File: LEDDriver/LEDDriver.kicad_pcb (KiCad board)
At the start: 2 copper layers, 39.4 x 41.9 mm, 16 parts, among them CON1 36V DC Power, P1 En, P2 ToLED, P3 To5V Power, Q1 Q_PMOS_GDS

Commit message: lestarch: adding design files for combined design v2.0
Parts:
- removed C2: Cf, Capacitors_SMD:C_0805
- removed C3: Cin, Capacitors_SMD:C_0603
- removed C4: CP, Capacitors_ThroughHole:C_Radial_D10_L16_P5
- removed CON1: 36V DC Power, footprints:PJ-051A
- removed D1: D_Schottky, Diodes_ThroughHole:Diode_DO-41_SOD81_Horizontal_RM10
- removed L1: INDUCTOR, footprints:SLF6045
- removed LM1: lm3409, Housings_DIP:DIP-14_W7.62mm
- removed P1: En, Pin_Headers:Pin_Header_Straight_1x01
- removed P2: ToLED, Pin_Headers:Pin_Header_Straight_1x02
- removed P3: To5V Power, Pin_Headers:Pin_Header_Straight_1x02
- removed Q1: Q_PMOS_GDS, footprints:TO-252-3
- removed R1: Roff, Resistors_SMD:R_1210
- removed R2: Ruv1, Resistors_SMD:R_1210
- removed R3: Ruv2, Resistors_SMD:R_0805
- removed R4: Rsns, footprints:R_1020
- added 110u: CP, Capacitors_ThroughHole:C_Radial_D10_L16_P5, F.Cu at (162.6, 88.9)
- added 1k: R, Resistors_SMD:R_0402, F.Cu at (142.2, 104.8)
- added 1k: R, Resistors_SMD:R_0402, F.Cu at (144.1, 104.8)
- added 30V,GND: ToLED, Pin_Headers:Pin_Header_Straight_1x02, F.Cu at (165.7, 112.4)
- added 330u: 330u, Capacitors_ThroughHole:C_Radial_D10_L16_P5, F.Cu at (135.9, 76.2)
- added 36V DC: 36V DC Power, footprints:PJ-051A, F.Cu at (163.2, 76.2)
- added 5V,GND: FanOut, Pin_Headers:Pin_Header_Straight_1x02, F.Cu at (129.5, 111.8)
- added Cf: Cf, Capacitors_SMD:C_0805, F.Cu at (156.8, 90.8)
- added Cin: Cin, Capacitors_SMD:C_0603, F.Cu at (156.8, 87.0)
- added D: D_Schottky, Diodes_ThroughHole:Diode_DO-41_SOD81_Horizontal_RM10, F.Cu at (168.3, 107.3)
- added D: D_Schottky, Diodes_ThroughHole:Diode_DO-41_SOD81_Horizontal_RM10, F.Cu at (144.1, 84.5)
- added Fan,LED,GND,5V: TeensyConnector, Pin_Headers:Pin_Header_Straight_1x04, F.Cu at (129.5, 92.1)
- added L15u: INDUCTOR, footprints:SLF6045, F.Cu at (159.4, 109.9)
- added L330u: 330u, Resistors_ThroughHole:Resistor_Horizontal_RM25mm, F.Cu at (136.5, 84.5)
- added NMOS: Q_NMOS_GDS, footprints:TO-252-3, F.Cu at (144.1, 110.5)
- added PMOS: Q_PMOS_GDS, footprints:TO-252-3, F.Cu at (163.2, 102.2)
- added Roff: Roff, Resistors_SMD:R_1210, F.Cu at (153.7, 111.1)
- added Rsns: Rsns, footprints:R_1020, F.Cu at (159.4, 96.5)
- added Ruv1: Ruv1, Resistors_SMD:R_1210, F.Cu at (151.1, 83.8)
- added Ruv2: Ruv2, Resistors_SMD:R_0805, F.Cu at (155.6, 83.8)
- added TL2575: TL25527, footprints:TO-263, F.Cu at (154.3, 76.2)
- added lm3409: lm3409, Housings_DIP:DIP-14_W7.62mm, F.Cu at (146.7, 89.5)
- moved C1 33.6 mm to (144.8, 101.6)
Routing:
- net /Regulator1/5VOut: track 0.00 -> 88.5 mm
- net VCC: track 75.7 -> 36.8 mm
- net Net-(D201-Pad1): track 0.00 -> 21.6 mm
- net Net-(P3-Pad4): track 0.00 -> 17.0 mm
- net Net-(Q2-Pad1): track 0.00 -> 13.3 mm
- net Net-(P1-Pad2): track 0.00 -> 12.6 mm
- net Net-(LM1-Pad4): track 5.08 -> 17.1 mm
- net GND: track 155.8 -> 147.2 mm, vias 3 -> 6
- net Net-(D1-Pad1): track 9.04 -> 16.7 mm
- net Net-(C1-Pad1): track 10.3 -> 17.2 mm
- net Net-(LM1-Pad1): track 14.1 -> 12.1 mm
- net Net-(C2-Pad2): track 4.45 -> 3.86 mm
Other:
- board size 39.4 x 41.9 mm -> 44.5 x 46.4 mm
- net class Default: trace_width 0.25 -> 0.5; via_dia 0.6 -> 0.8
- rule pad_to_mask_clearance: 0.2 -> 0
- board text added: "LeStarch 2016 - Combined circuit for micro- controller driven LED lamp. - LED Driver 30V, 1A - Regulator 5V, ~1A - NMOS GND switch"
- board text removed: "LED driver: Vin - 36V, Vout - 30V, Iout - 1A LEDs need a constant current and thus cannot be driven given just a voltage, but rather must be driven to maintain constant current."
- board text removed: "LeStarch 2015"

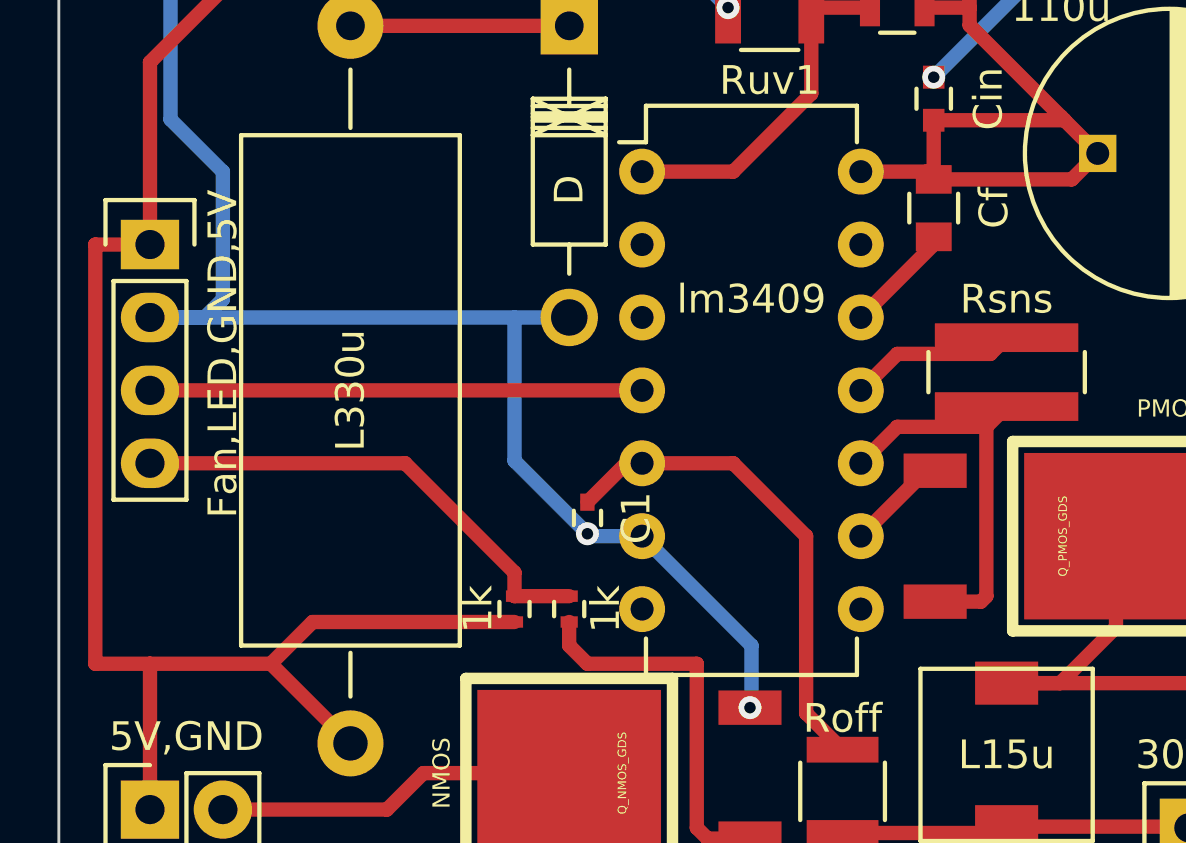
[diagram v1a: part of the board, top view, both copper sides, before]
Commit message: lestarch: changing resistors to pulldown resistors; adding pulldown to LED
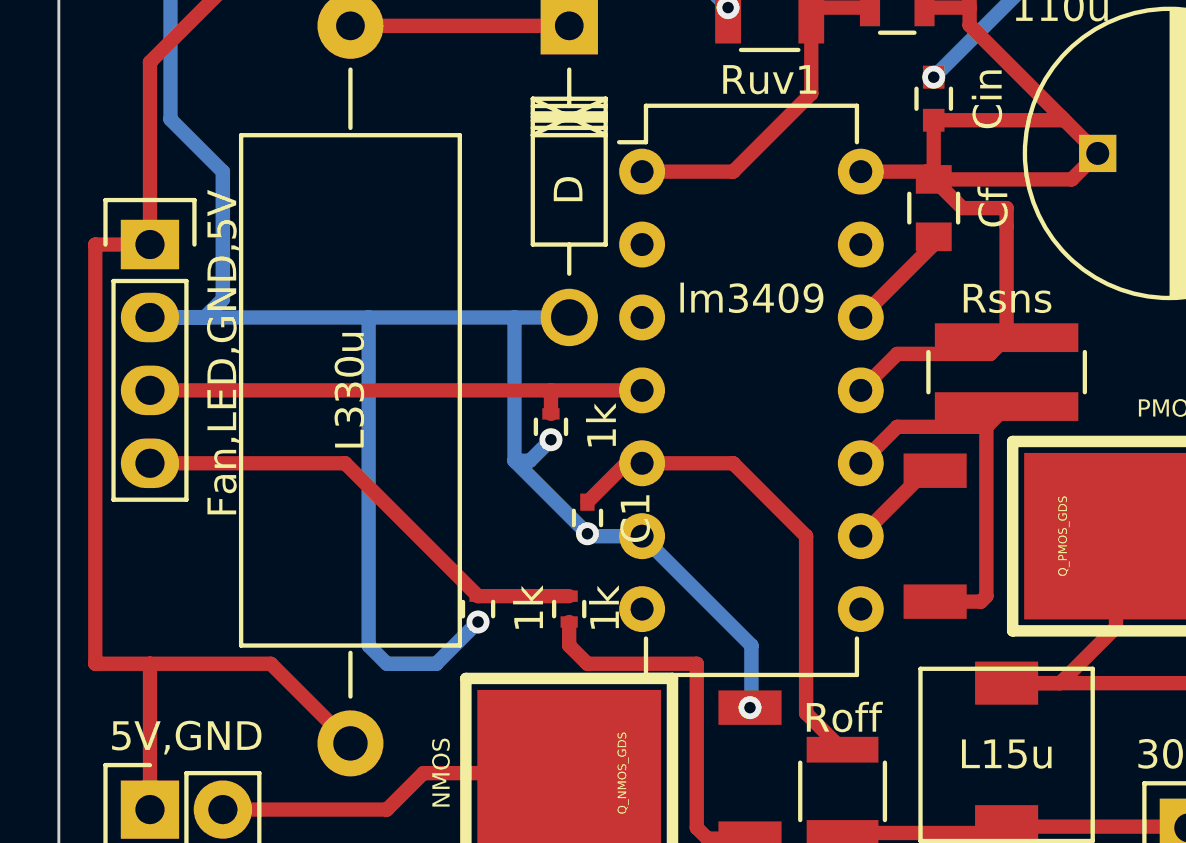
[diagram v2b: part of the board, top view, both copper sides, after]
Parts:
- removed the 1k at (142.2, 104.8)
- added 1k: R, Resistors_SMD:R_0402, F.Cu at (141.0, 104.8)
- added 1k: R, Resistors_SMD:R_0402, F.Cu at (143.5, 98.4)
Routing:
- net GND: track 147.2 -> 164.9 mm, vias 6 -> 8
- net /Regulator1/5VOut: track 88.5 -> 79.4 mm
- net VCC: track 36.8 -> 44.2 mm
- net Net-(LM1-Pad4): track 17.1 -> 18.0 mm
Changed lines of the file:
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@@
 (kicad_pcb (version 4) (host pcbnew 4.0.4+e1-6308~48~ubuntu16.04.1-stable)
   (general
-    (links 46)
-    (no_connects 1)
-    (area 114.846904 20.03 163.63246 65.890476)
+    (links 48)
+    (no_connects 0)
+    (area 126.314999 68.529999 170.865001 114.985001)
     (thickness 1.6)
     (drawings 6)
-    (tracks 131)
+    (tracks 143)
     (zones 0)
-    (modules 23)
+    (modules 24)
     (nets 21)
   )
@@
   (layers
     (0 F.Cu signal)
-    (31 B.Cu signal hide)
+    (31 B.Cu signal)
     (32 B.Adhes user hide)
     (33 F.Adhes user hide)
     (34 B.Paste user hide)
     (35 F.Paste user hide)
-    (36 B.SilkS user)
+    (36 B.SilkS user hide)
     (37 F.SilkS user)
     (38 B.Mask user hide)
@@
     (add_net "Net-(Q2-Pad1)")
     (add_net VCC)
+  )
+  (module Resistors_SMD:R_0402 (layer F.Cu)
+    (at 140.97 104.775 270)
+    (descr "Resistor SMD 0402, reflow soldering, Vishay (see dcrcw.pdf)")
+    (tags "resistor 0402")
+    (attr smd)
+    (fp_text reference 1k (at 0 -1.8 270) (layer F.SilkS)
+      (effects (font (size 1 1) (thickness 0.15)))
+    )
+    (fp_text value R (at 0 1.8 270) (layer F.Fab)
+      (effects (font (size 1 1) (thickness 0.15)))
+    )
+    (fp_line (start -0.95 -0.65) (end 0.95 -0.65) (layer F.CrtYd) (width 0.05))
+    (fp_line (start -0.95 0.65) (end 0.95 0.65) (layer F.CrtYd) (width 0.05))
+    (fp_line (start -0.95 -0.65) (end -0.95 0.65) (layer F.CrtYd) (width 0.05))
+    (fp_line (start 0.95 -0.65) (end 0.95 0.65) (layer F.CrtYd) (width 0.05))
+    (fp_line (start 0.25 -0.525) (end -0.25 -0.525) (layer F.SilkS) (width 0.15))
+    (fp_line (start -0.25 0.525) (end 0.25 0.525) (layer F.SilkS) (width 0.15))
+    (pad 1 smd rect (at -0.45 0 270) (size 0.4 0.6) (layers F.Cu F.Paste F.Mask)
+      (net 19 "Net-(P3-Pad4)"))
+    (pad 2 smd rect (at 0.45 0 270) (size 0.4 0.6) (layers F.Cu F.Paste F.Mask)
+      (net 2 GND))
+    (model Resistors_SMD.3dshapes/R_0402.wrl
+      (at (xyz 0 0 0))
+      (scale (xyz 1 1 1))
+      (rotate (xyz 0 0 0))
+    )
   )
   (module Capacitors_SMD:C_0402 (layer F.Cu)
@@
   )
   (module Resistors_SMD:R_0402 (layer F.Cu)
-    (at 142.24 104.775 270)
-    (descr "Resistor SMD 0402, reflow soldering, Vishay (see dcrcw.pdf)")
-    (tags "resistor 0402")
-    (attr smd)
-    (fp_text reference 1k (at 0 1.27 270) (layer F.SilkS)
-      (effects (font (size 1 1) (thickness 0.15)))
-    )
-    (fp_text value R (at 0 1.8 270) (layer F.Fab)
-      (effects (font (size 1 1) (thickness 0.15)))
-    )
-    (fp_line (start -0.95 -0.65) (end 0.95 -0.65) (layer F.CrtYd) (width 0.05))
-    (fp_line (start -0.95 0.65) (end 0.95 0.65) (layer F.CrtYd) (width 0.05))
-    (fp_line (start -0.95 -0.65) (end -0.95 0.65) (layer F.CrtYd) (width 0.05))
-    (fp_line (start 0.95 -0.65) (end 0.95 0.65) (layer F.CrtYd) (width 0.05))
-    (fp_line (start 0.25 -0.525) (end -0.25 -0.525) (layer F.SilkS) (width 0.15))
-    (fp_line (start -0.25 0.525) (end 0.25 0.525) (layer F.SilkS) (width 0.15))
-    (pad 1 smd rect (at -0.45 0 270) (size 0.4 0.6) (layers F.Cu F.Paste F.Mask)
-      (net 19 "Net-(P3-Pad4)"))
-    (pad 2 smd rect (at 0.45 0 270) (size 0.4 0.6) (layers F.Cu F.Paste F.Mask)
-      (net 5 /Regulator1/5VOut))
-    (model Resistors_SMD.3dshapes/R_0402.wrl
-      (at (xyz 0 0 0))
-      (scale (xyz 1 1 1))
-      (rotate (xyz 0 0 0))
-    )
-  )
-  (module Resistors_SMD:R_0402 (layer F.Cu)
     (at 144.145 104.775 270)
     (descr "Resistor SMD 0402, reflow soldering, Vishay (see dcrcw.pdf)")
@@
     (pad "" smd rect (at 0 -10.67 90) (size 10.8 7) (layers F.Cu F.Paste F.Mask))
   )
+  (module Resistors_SMD:R_0402 (layer F.Cu)
+    (at 143.51 98.425 270)
+    (descr "Resistor SMD 0402, reflow soldering, Vishay (see dcrcw.pdf)")
+    (tags "resistor 0402")
+    (attr smd)
+    (fp_text reference 1k (at 0 -1.8 270) (layer F.SilkS)
+      (effects (font (size 1 1) (thickness 0.15)))
+    )
+    (fp_text value R (at 0 1.8 270) (layer F.Fab)
+      (effects (font (size 1 1) (thickness 0.15)))
+    )
+    (fp_line (start -0.95 -0.65) (end 0.95 -0.65) (layer F.CrtYd) (width 0.05))
+    (fp_line (start -0.95 0.65) (end 0.95 0.65) (layer F.CrtYd) (width 0.05))
+    (fp_line (start -0.95 -0.65) (end -0.95 0.65) (layer F.CrtYd) (width 0.05))
+    (fp_line (start 0.95 -0.65) (end 0.95 0.65) (layer F.CrtYd) (width 0.05))
+    (fp_line (start 0.25 -0.525) (end -0.25 -0.525) (layer F.SilkS) (width 0.15))
+    (fp_line (start -0.25 0.525) (end 0.25 0.525) (layer F.SilkS) (width 0.15))
+    (pad 1 smd rect (at -0.45 0 270) (size 0.4 0.6) (layers F.Cu F.Paste F.Mask)
+      (net 12 "Net-(LM1-Pad4)"))
+    (pad 2 smd rect (at 0.45 0 270) (size 0.4 0.6) (layers F.Cu F.Paste F.Mask)
+      (net 2 GND))
+    (model Resistors_SMD.3dshapes/R_0402.wrl
+      (at (xyz 0 0 0))
+      (scale (xyz 1 1 1))
+      (rotate (xyz 0 0 0))
+    )
+  )
   (gr_text "LeStarch 2016 -\n  Combined circuit for micro-\n  controller driven LED lamp.\n    - LED Driver 30V, 1A\n    - Regulator 5V, ~1A\n    - NMOS GND switch" (at 166.37 90.805) (layer B.SilkS)
     (effects (font (size 1.5 1.5) (thickness 0.3)) (justify left mirror))
@@
   (segment (start 146.685 99.695) (end 146.135 99.695) (width 0.5) (layer F.Cu) (net 1))
   (segment (start 146.135 99.695) (end 144.78 101.05) (width 0.5) (layer F.Cu) (net 1))
+  (via (at 140.97 105.225) (size 0.8) (drill 0.4) (layers F.Cu B.Cu) (net 2) (status C00000))
+  (segment (start 137.16 94.615) (end 137.16 106.045) (width 0.5) (layer B.Cu) (net 2))
+  (segment (start 137.795 106.68) (end 137.16 106.045) (width 0.5) (layer B.Cu) (net 2))
+  (segment (start 139.515 106.68) (end 137.795 106.68) (width 0.5) (layer B.Cu) (net 2))
+  (segment (start 139.515 106.68) (end 140.97 105.225) (width 0.5) (layer B.Cu) (net 2) (status 800000))
+  (via (at 143.51 98.875) (size 0.8) (drill 0.4) (layers F.Cu B.Cu) (net 2))
+  (segment (start 142.24 99.61) (end 142.775 99.61) (width 0.5) (layer B.Cu) (net 2))
+  (segment (start 142.775 99.61) (end 143.51 98.875) (width 0.5) (layer B.Cu) (net 2))
   (segment (start 146.05 82.55) (end 148.41 82.55) (width 0.5) (layer B.Cu) (net 2))
   (segment (start 148.41 82.55) (end 149.68 83.82) (width 0.5) (layer B.Cu) (net 2))
@@
   (segment (start 150.495 108.15828) (end 150.495 106.045) (width 0.5) (layer B.Cu) (net 2))
   (segment (start 146.685 102.235) (end 150.495 106.045) (width 0.5) (layer B.Cu) (net 2))
-  (segment (start 129.54 94.615) (end 142.24 94.615) (width 0.5) (layer B.Cu) (net 2))
+  (segment (start 129.54 94.615) (end 137.16 94.615) (width 0.5) (layer B.Cu) (net 2))
+  (segment (start 137.16 94.615) (end 142.24 94.615) (width 0.5) (layer B.Cu) (net 2))
   (segment (start 142.24 94.615) (end 144.14754 94.615) (width 0.5) (layer B.Cu) (net 2))
   (segment (start 130.255 82.55) (end 130.255 87.71) (width 0.5) (layer B.Cu) (net 2))
@@
   (via (at 154.305 76.2) (size 0.8) (drill 0.4) (layers F.Cu B.Cu) (net 2))
   (via (at 156.845 86.245) (size 0.8) (drill 0.4) (layers F.Cu B.Cu) (net 2))
+  (segment (start 159.385 90.805) (end 157.845 90.805) (width 0.5) (layer F.Cu) (net 3))
+  (segment (start 159.385 95.32) (end 159.385 91.44) (width 0.5) (layer F.Cu) (net 3))
+  (segment (start 159.385 90.805) (end 159.385 91.44) (width 0.5) (layer F.Cu) (net 3))
+  (segment (start 157.845 90.805) (end 156.845 89.805) (width 0.5) (layer F.Cu) (net 3))
   (segment (start 158.095 83.82) (end 156.525 83.82) (width 0.5) (layer F.Cu) (net 3))
   (segment (start 154.305 97.155) (end 155.575 95.885) (width 0.5) (layer F.Cu) (net 3))
@@
   (segment (start 156.845 91.805) (end 156.845 92.075) (width 0.5) (layer F.Cu) (net 4))
   (segment (start 156.845 92.075) (end 154.305 94.615) (width 0.5) (layer F.Cu) (net 4))
-  (segment (start 142.24 105.225) (end 135.20632 105.225) (width 0.5) (layer F.Cu) (net 5))
-  (segment (start 135.20632 105.225) (end 133.75132 106.68) (width 0.5) (layer F.Cu) (net 5))
   (segment (start 129.54 111.76) (end 129.54 106.68) (width 0.5) (layer F.Cu) (net 5))
   (segment (start 127.635 106.68) (end 129.54 106.68) (width 0.5) (layer F.Cu) (net 5))
@@
   (segment (start 149.86 89.535) (end 152.58 86.815) (width 0.5) (layer F.Cu) (net 9))
   (segment (start 154.625 83.82) (end 152.58 83.82) (width 0.5) (layer F.Cu) (net 9))
-  (segment (start 129.54 97.155) (end 146.685 97.155) (width 0.5) (layer F.Cu) (net 12))
+  (segment (start 143.51 97.975) (end 143.51 97.155) (width 0.5) (layer F.Cu) (net 12))
+  (segment (start 129.54 97.155) (end 143.51 97.155) (width 0.5) (layer F.Cu) (net 12))
+  (segment (start 143.51 97.155) (end 146.685 97.155) (width 0.5) (layer F.Cu) (net 12))
   (segment (start 156.8958 99.95408) (end 156.58592 99.95408) (width 0.5) (layer F.Cu) (net 15))
   (segment (start 156.58592 99.95408) (end 154.305 102.235) (width 0.5) (layer F.Cu) (net 15))
@@
   (segment (start 137.795 111.76) (end 132.08 111.76) (width 0.5) (layer F.Cu) (net 18))
   (segment (start 139.065 110.49) (end 137.795 111.76) (width 0.5) (layer F.Cu) (net 18))
-  (segment (start 142.24 104.325) (end 144.145 104.325) (width 0.5) (layer F.Cu) (net 19))
-  (segment (start 142.24 104.325) (end 142.24 103.505) (width 0.5) (layer F.Cu) (net 19))
-  (segment (start 138.43 99.695) (end 129.54 99.695) (width 0.5) (layer F.Cu) (net 19))
-  (segment (start 142.24 103.505) (end 138.43 99.695) (width 0.5) (layer F.Cu) (net 19))
+  (segment (start 140.97 104.325) (end 144.145 104.325) (width 0.5) (layer F.Cu) (net 19) (status C00000))
+  (segment (start 129.54 99.695) (end 136.34 99.695) (width 0.5) (layer F.Cu) (net 19) (status 400000))
+  (segment (start 136.34 99.695) (end 140.97 104.325) (width 0.5) (layer F.Cu) (net 19) (status 800000))
   (segment (start 144.145 105.225) (end 144.145 106.045) (width 0.5) (layer F.Cu) (net 20))
   (segment (start 148.96592 112.77092) (end 150.4442 112.77092) (width 0.5) (layer F.Cu) (net 20))
